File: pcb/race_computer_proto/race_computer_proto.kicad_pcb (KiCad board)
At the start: 4 copper layers, 121.2 x 73.5 mm, 18 parts, among them U1 Teensy4.0, U3 SN74LVC245APW, U8 74LS125

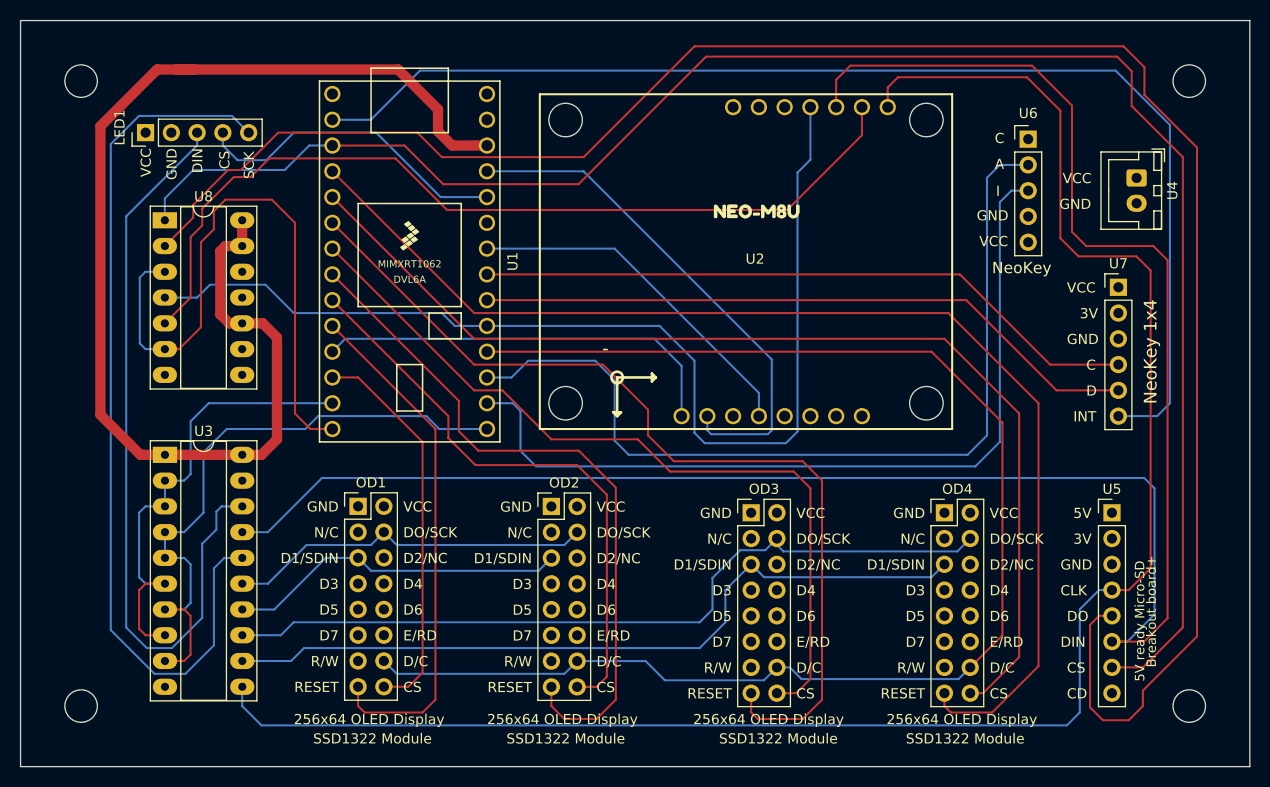
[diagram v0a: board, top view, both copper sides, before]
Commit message: Update PCB to account for second SPI connection -- note that the initial routing was just thrown together and needs to be reviewed and cleaned up.
Remove doSPILock()/doSPIUnlock() calls from storage code as they are not needed anymore.

Add timezone definitions and a timeDateSettings class to handle the timezone.  Still need to add menu to configure timezone.
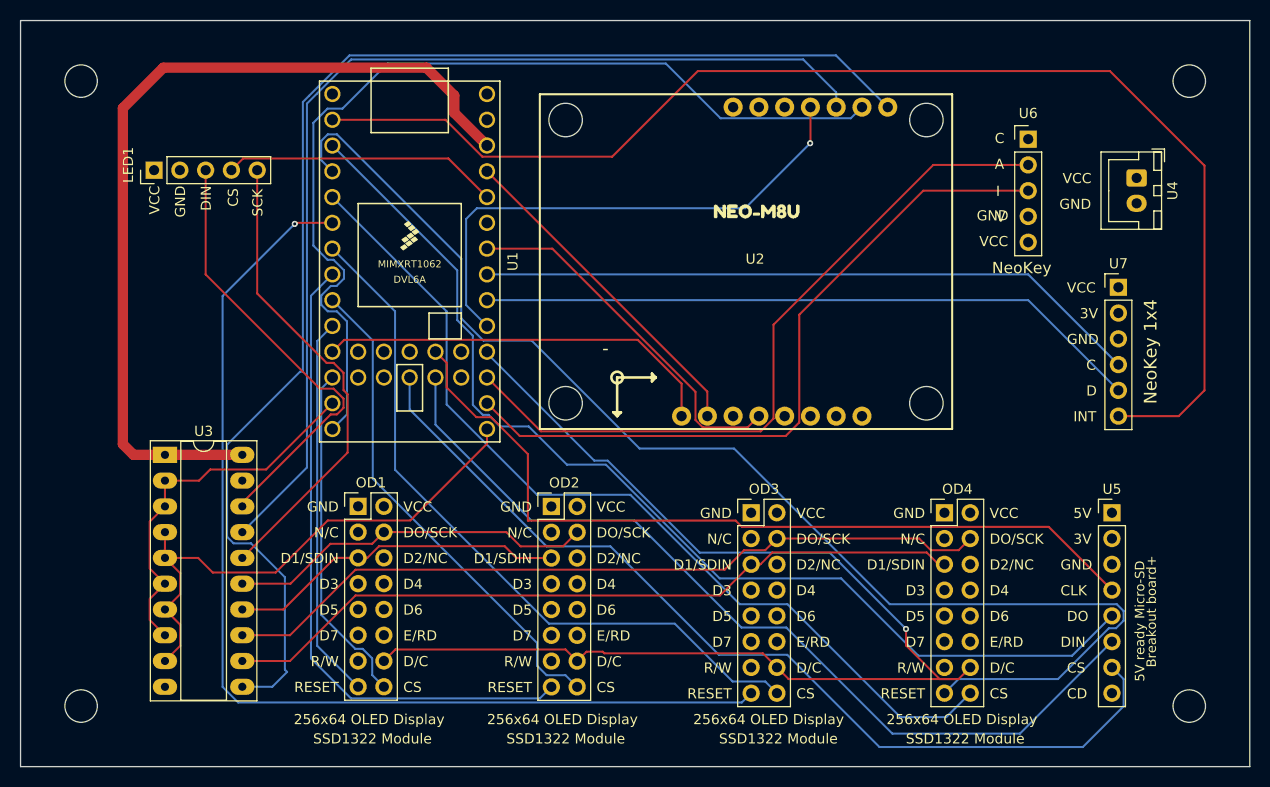
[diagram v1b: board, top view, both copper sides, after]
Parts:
- removed U8: 74LS125, Package_DIP:DIP-14_W7.62mm_Socket_LongPads
- U1: footprint race_computer:teensy4_0_reduced -> race_computer:Teensy40_reduced1
- moved LED1 3.79 mm to (104.3, 83.7)
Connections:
- U1 pad 3: /SDCARD_CS -> Net-(U1-1_TX1_CTX2_MISO1)
- U2 pad 10: Net-(U2-TX/MISO) -> /MISO
- U5 pad 4: /GPS_SD_SCK -> Net-(U1-27_A13_SCK1)
- U5 pad 5: Net-(U5-DO) -> Net-(U1-1_TX1_CTX2_MISO1)
- U5 pad 6: /GPS_SD_MOSI -> Net-(U1-26_A12_MOSI1)
- U5 pad 7: /SDCARD_CS -> Net-(U1-28_RX7)
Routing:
- net Net-(U5-DO): track 192.6 -> 0.00 mm
- net /SDCARD_CS: track 172.5 -> 0.00 mm
- net Net-(U1-1_TX1_CTX2_MISO1): track 0.00 -> 106.2 mm
- net /GPS_SD_MOSI: track 203.2 -> 101.6 mm
- net Net-(U1-28_RX7): track 0.00 -> 93.3 mm
- net Net-(U2-TX/MISO): track 87.8 -> 0.00 mm
- net Net-(U1-26_A12_MOSI1): track 0.00 -> 87.7 mm
- net Net-(U1-27_A13_SCK1): track 0.00 -> 81.7 mm
- net Net-(U1-17_A3_TX4_SDA1): track 106.5 -> 52.0 mm, vias 0 -> 1
- net /GPS_SD_SCK: track 177.4 -> 129.6 mm
- net /DISP_BUS.SCK2: track 87.3 -> 46.6 mm
- net /3V3: track 122.4 -> 87.1 mm
- net /MISO: track 60.8 -> 94.4 mm
- net /DISP_BUS.MOSI2: track 75.0 -> 44.1 mm
- net /DISP_BUS.DC: track 140.2 -> 121.6 mm, vias 0 -> 1
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
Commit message: Fairly substantial change set that brings in PCB changes from re-routing the board supporting a second SPI port dedicated to the SD card.  Still needs review and testing of all the new pin assignments to ensure everything supports what has been assigned to it -- not all pins can be used for all counters, etc.  Also begins a bunch of code cleanup.  The code was thrown together in a "it works, move on" paradigm, with some thought to the future, but not a lot.  This starts the clean up to make things more supportable long term, and hopefully easier to add features to.  The fixes here are minor, but a start.
Removed the original test code that started the whole project.  It was a mash of library
examples and thrown together code that wouldn't run on anything.

Added a GPS synced clock -- very very simple.  Used the same GPS module and LED display.
It has enough functionality to ensure that the race computer was starting in sync with
GPS time when in delayed start mode.  It is.  Will leave the code here though as it may
be useful in the future.

More details updates and fixes follow.

pcb: update race computer prototype to revision 3.0

- Bump PCB revision from 2.2 to 3.0

- Add J3 (2-pin JST XH) wheel speed sensor input connector and optocoupler
  isolation from microcontroller.  Wheel speed input is designed to be driven
  for an open collector driver.

- Add J1 (3-pin JST XH) I2C communication breakout connector.  Options for future
  expansion.

- Add J2 (3-pin JST XH) serial communication breakout connector.  Options for
  future expandsion

- Reposition headers

- Reorganize net assignments throughout the board to simplify routing.  Will
  require code updates when switching to new board.  Need to confirm all pins
  support their expected functionality.

refactor: encapsulate OLED displays into display_t objects

- Introduce display class that wraps U8G2 display objects, each
  managing its own content list instead of a single global list

- Replace raw buffer poin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
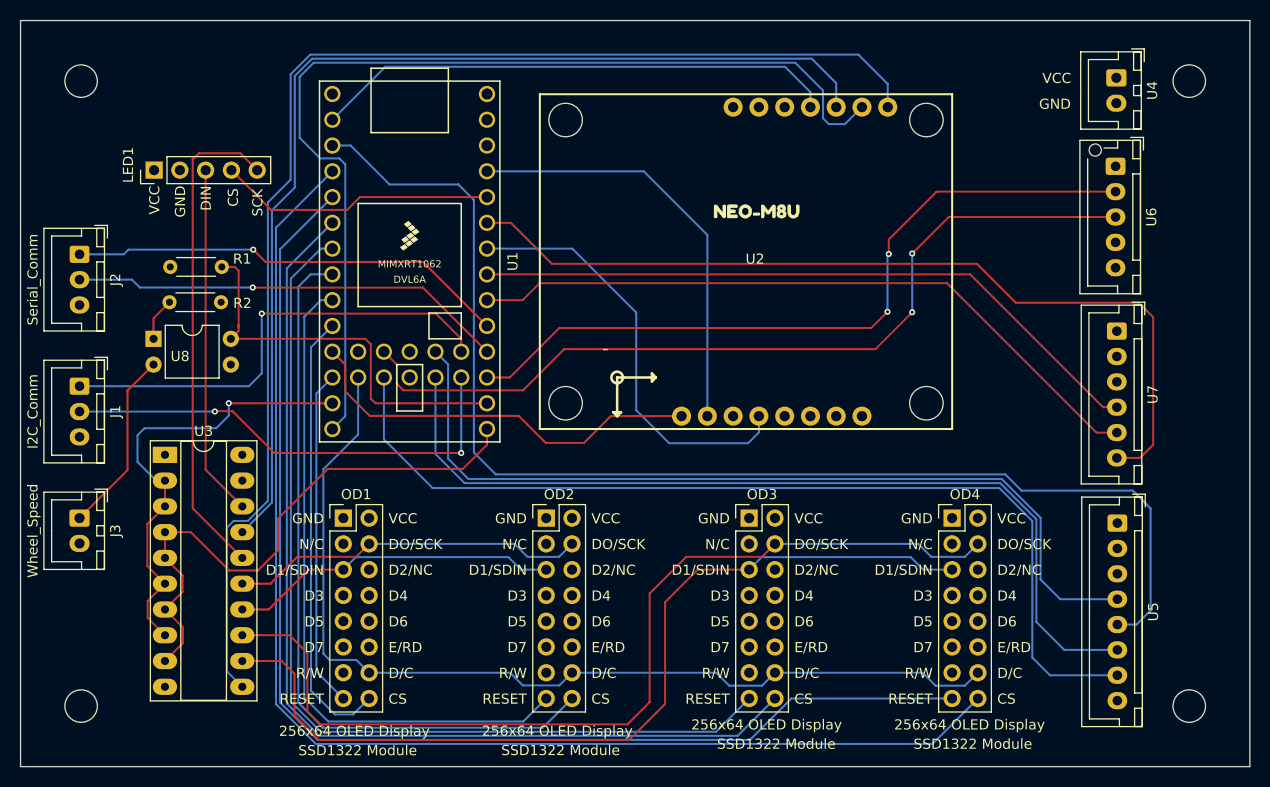
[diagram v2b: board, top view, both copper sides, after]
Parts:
- added J1: I2C_Comm, Connector_JST:JST_XH_B3B-XH-A_1x03_P2.50mm_Vertical, F.Cu at (97.0, 105.0)
- added J2: Serial_Comm, Connector_JST:JST_XH_B3B-XH-A_1x03_P2.50mm_Vertical, F.Cu at (97.0, 92.0)
- added J3: Wheel_Speed, Connector_JST:JST_XH_B2B-XH-A_1x02_P2.50mm_Vertical, F.Cu at (97.0, 118.0)
- added R1: 10K, Resistor_THT:R_Axial_DIN0204_L3.6mm_D1.6mm_P5.08mm_Horizontal, F.Cu at (111.0, 93.2)
- added R2: 1K, Resistor_THT:R_Axial_DIN0204_L3.6mm_D1.6mm_P5.08mm_Horizontal, F.Cu at (110.9, 96.7)
- added U8: EL817, Package_DIP:DIP-4_W7.62mm, F.Cu at (104.3, 100.3)
- U5: footprint race_computer:microsd_breakout_header -> Connector_JST:JST_XH_B8B-XH-A_1x08_P2.50mm_Vertical
- U6: footprint race_computer:neokey_header -> Connector_JST:JST_XH_B5B-XH-AM_1x05_P2.50mm_Vertical
- U7: footprint race_computer:neokey_1x4_header -> Connector_JST:JST_XH_B6B-XH-A_1x06_P2.50mm_Vertical
- moved U4 10.1 mm to (199.2, 74.6)
- moved U6 9.02 mm to (199.1, 83.3), turned to -90 degrees
- moved U7 4.32 mm to (199.2, 99.6), turned to -90 degrees
- moved OD1 1.86 mm to (123.0, 118.0)
- moved OD2 1.25 mm to (143.0, 118.0)
- moved U5 1.15 mm to (199.3, 118.5), turned to -90 degrees
- moved OD4 0.92 mm to (183.0, 118.0)
- moved OD3 0.56 mm to (163.0, 118.0)
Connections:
- U1 pad 10: /DISP_BUS.RESET0 -> /DISP_BUS.CS0
- U1 pad 12: /DISP_BUS.CS0 -> /DISP_BUS.RESET0
- U1 pad 2: /NEOKEY_INT -> /GPS_CS
- U1 pad 23: /DISP_BUS.DC -> Net-(J2-Pin_2)
- U1 pad 24: Net-(U1-17_A3_TX4_SDA1) -> Net-(J2-Pin_1)
- U1 pad 28: unconnected-(U1-21_A7_RX5_BCLK1-Pad28) -> /NEOKEY_INT
- U1 pad 35: unconnected-(U1-24_A10_TX6_SCL2-Pad35) -> Net-(J1-Pin_2)
- U1 pad 36: unconnected-(U1-25_A11_RX6_SDA2-Pad36) -> Net-(J1-Pin_1)
- U1 pad 39: Net-(U1-28_RX7) -> unconnected-(U1-28_RX7-Pad39)
- U1 pad 4: /DISP_BUS.RESET3 -> /DISP_BUS.CS3
- U1 pad 41: unconnected-(U1-30_CRX3-Pad41) -> Net-(U1-30_CRX3)
- U1 pad 42: unconnected-(U1-31_CTX3-Pad42) -> Net-(U1-31_CTX3)
- U1 pad 43: unconnected-(U1-32_OUT1B-Pad43) -> /DISP_BUS.DC
- U1 pad 5: /DISP_BUS.CS3 -> /DISP_BUS.RESET3
- U1 pad 6: /DISP_BUS.RESET2 -> /DISP_BUS.CS2
- U1 pad 7: /DISP_BUS.CS2 -> /DISP_BUS.RESET2
- U1 pad 8: /DISP_BUS.RESET1 -> /DISP_BUS.CS1
- U1 pad 9: /DISP_BUS.CS1 -> /DISP_BUS.RESET1
- U2 pad 12: Net-(U1-17_A3_TX4_SDA1) -> /GPS_CS
- U5 pad 7: Net-(U1-28_RX7) -> Net-(U1-30_CRX3)
- U6 pad 3: Net-(U1-14_A0_TX3_SPDIF_OUT) -> Net-(U1-31_CTX3)
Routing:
- net Net-(U1-30_CRX3): track 0.00 -> 95.9 mm
- net Net-(U1-28_RX7): track 93.3 -> 0.00 mm
- net Net-(U1-31_CTX3): track 0.00 -> 85.3 mm, vias 0 -> 2
- net Net-(U1-17_A3_TX4_SDA1): track 52.0 -> 0.00 mm, vias 1 -> 0
- net /GPS_CS: track 0.00 -> 51.8 mm
- net Net-(J1-Pin_2): track 0.00 -> 46.8 mm, vias 0 -> 2
- net Net-(J1-Pin_1): track 0.00 -> 46.3 mm, vias 0 -> 1
- net Net-(J2-Pin_1): track 0.00 -> 43.5 mm, vias 0 -> 1
- net Net-(J2-Pin_2): track 0.00 -> 43.1 mm, vias 0 -> 1
- net /NEOKEY_INT: track 126.5 -> 86.2 mm
- net /DISP_BUS.CS3: track 90.4 -> 127.5 mm
- net Net-(U1-14_A0_TX3_SPDIF_OUT): track 70.9 -> 40.3 mm
- net /DISP_BUS.CS2: track 71.1 -> 100.2 mm
- net /DISP_BUS.CS1: track 49.2 -> 74.1 mm
- net /DISP_BUS.DC: track 121.6 -> 97.1 mm, vias 1 -> 0
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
